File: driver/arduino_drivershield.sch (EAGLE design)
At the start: 35 parts, among them IC1 LB1973M, IC10 LB1973M, IC11 LB1973M, IC12 74HC14D, IC2 LB1973M, IC3 74HC14D, IC4 LB1973M, IC5 LB1973M, IC6 74HC14D, IC7 LB1973M, IC8 LB1973M, IC9 74HC14D, J1 J5MM, J2 J5MM, U1 ARDUINO_SHIELDLABEL

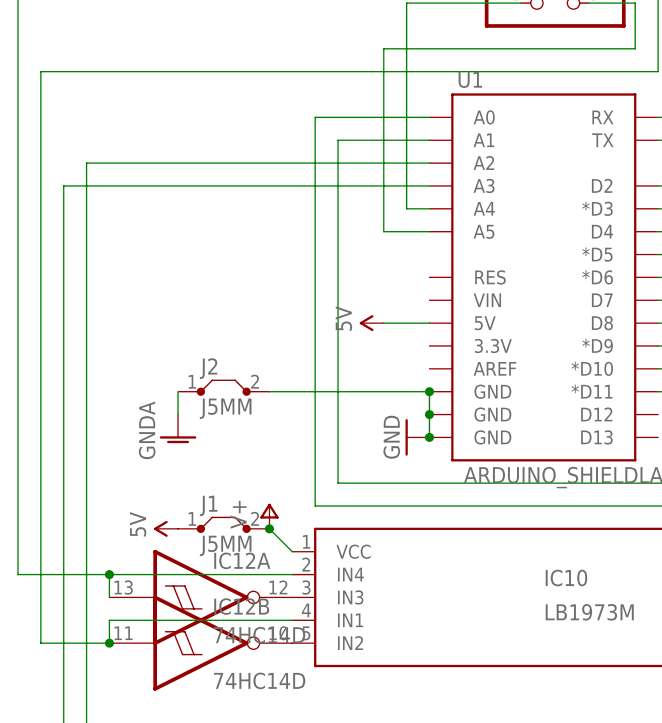
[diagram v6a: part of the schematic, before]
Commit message: added some more jumper to hopefully get better ground connections
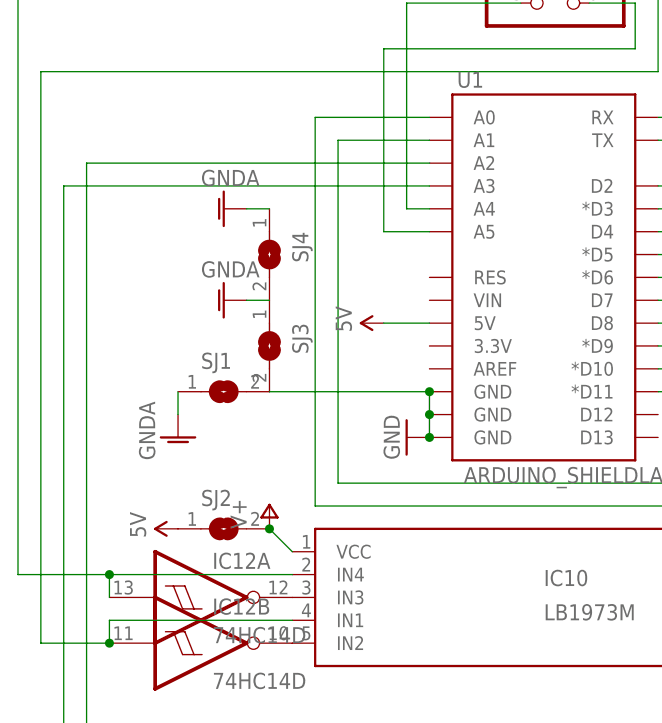
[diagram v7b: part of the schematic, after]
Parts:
- removed J1, J2: J5MM, jumper:J5MM
- added SJ1, SJ2, SJ3, SJ4: (no value), jumper:SJ
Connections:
- removed net GND@2: C10.1, C11.1, C9.1, IC12C.I, IC12D.I, IC12P.GND, IC3C.I, IC3D.I, IC3P.GND, IC6C.I, IC6D.I, IC6P.GND, IC9C.I, IC9D.I, IC9P.GND, J2.2, U1.GND@0, U1.GND@1, U1.GND@2
- removed net GND@3: C1.2, C2.2, C3.2, C4.2, C5.2, C6.2, C7.2, C8.2, IC1.GND, IC10.GND, IC11.GND, IC2.GND, IC4.GND, IC5.GND, IC7.GND, IC8.GND, J2.1
- new net FOO: C1.2, C2.2, C3.2, C4.2, C5.2, C6.2, C7.2, C8.2, IC1.GND, IC11.GND, IC2.GND, IC4.GND, IC5.GND, IC7.GND, IC8.GND, SJ1.1, SJ3.1, SJ4.1
- new net GND: C10.1, C11.1, C9.1, IC12C.I, IC12D.I, IC12P.GND, IC3C.I, IC3D.I, IC3P.GND, IC6C.I, IC6D.I, IC6P.GND, IC9C.I, IC9D.I, IC9P.GND, SJ1.2, U1.GND@0, U1.GND@1, U1.GND@2
- new net GND@PWR: IC10.GND
- net 5V: now also SJ2.1
- net 5V@1: no longer J1.1
- net V+: now also SJ2.2; no longer J1.2
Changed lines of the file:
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@@
 <part name="P+7" library="supply1" deviceset="V+" device=""/>
 <part name="P+8" library="supply1" deviceset="V+" device=""/>
-<part name="J1" library="jumper" deviceset="J" device="5MM"/>
 <part name="U$3" library="SparkFun-Aesthetics" deviceset="5V" device=""/>
 <part name="GND14" library="supply1" deviceset="GNDA" device=""/>
@@
 <part name="P+15" library="supply1" deviceset="V+" device=""/>
 <part name="P+16" library="supply1" deviceset="V+" device=""/>
-<part name="J2" library="jumper" deviceset="J" device="5MM"/>
 <part name="GND9" library="supply1" deviceset="GNDA" device=""/>
 <part name="C9" library="rcl" deviceset="C-EU" device="C0805"/>
@@
 <part name="U$5" library="SparkFun-Aesthetics" deviceset="5V" device=""/>
 <part name="U$6" library="SparkFun-Aesthetics" deviceset="5V" device=""/>
+<part name="SJ1" library="jumper" deviceset="SJ" device=""/>
+<part name="SJ2" library="jumper" deviceset="SJ" device=""/>
+<part name="GND23" library="supply1" deviceset="GNDA" device=""/>
+<part name="SJ3" library="jumper" deviceset="SJ" device=""/>
+<part name="GND24" library="supply1" deviceset="GNDA" device=""/>
+<part name="SJ4" library="jumper" deviceset="SJ" device=""/>
 </parts>
 <sheets>
@@
 <instance part="P+7" gate="1" x="-2.54" y="-20.32"/>
 <instance part="P+8" gate="1" x="-5.08" y="5.08"/>
-<instance part="J1" gate="1" x="-10.16" y="2.54"/>
 <instance part="U$3" gate="G$1" x="-15.24" y="2.54" rot="R90"/>
 <instance part="GND14" gate="1" x="60.96" y="-35.56"/>
@@
 <instance part="P+15" gate="1" x="73.66" y="-20.32"/>
 <instance part="P+16" gate="1" x="73.66" y="2.54"/>
-<instance part="J2" gate="1" x="-10.16" y="17.78"/>
 <instance part="GND9" gate="1" x="-15.24" y="12.7"/>
 <instance part="C9" gate="G$1" x="58.42" y="109.22"/>
@@
 <instance part="U$5" gate="G$1" x="99.06" y="104.14" rot="R90"/>
 <instance part="U$6" gate="G$1" x="132.08" y="104.14" rot="R90"/>
+<instance part="SJ1" gate="1" x="-10.16" y="17.78"/>
+<instance part="SJ2" gate="1" x="-10.16" y="2.54"/>
+<instance part="GND23" gate="1" x="-10.16" y="27.94" rot="R270"/>
+<instance part="SJ3" gate="1" x="-5.08" y="22.86" rot="R270"/>
+<instance part="GND24" gate="1" x="-10.16" y="38.1" rot="R270"/>
+<instance part="SJ4" gate="1" x="-5.08" y="33.02" rot="R270"/>
 </instances>
 <busses>
@@
 <pinref part="IC12" gate="P" pin="VCC"/>
 <pinref part="U$13" gate="G$1" pin="5V"/>
-</segment>
-<segment>
-<pinref part="J1" gate="1" pin="1"/>
-<pinref part="U$3" gate="G$1" pin="5V"/>
 </segment>
 </net>
@@
 <pinref part="P+8" gate="1" pin="V+"/>
 <wire x1="-5.08" y1="2.54" x2="-2.54" y2="0" width="0.1524" layer="91"/>
-<pinref part="J1" gate="1" pin="2"/>
+<pinref part="SJ2" gate="1" pin="2"/>
 <junction x="-5.08" y="2.54"/>
 </segment>
@@
 </segment>
 </net>
-<net name="GND@3" class="1">
-<segment>
-<pinref part="IC10" gate="G$1" pin="GND"/>
-<pinref part="GND6" gate="1" pin="GNDA"/>
-<wire x1="60.96" y1="-12.7" x2="58.42" y2="-10.16" width="0.1524" layer="91"/>
-</segment>
+<net name="FOO" class="1">
 <segment>
 <pinref part="IC8" gate="G$1" pin="GND"/>
@@
 </segment>
 <segment>
-<pinref part="J2" gate="1" pin="1"/>
 <pinref part="GND9" gate="1" pin="GNDA"/>
 <wire x1="-15.24" y1="15.24" x2="-15.24" y2="17.78" width="0.1524" layer="91"/>
-</segment>
-</net>
-<net name="GND@2" class="0">
+<pinref part="SJ1" gate="1" pin="1"/>
+</segment>
+<segment>
+<pinref part="GND23" gate="1" pin="GNDA"/>
+<wire x1="-7.62" y1="27.94" x2="-5.08" y2="27.94" width="0.1524" layer="91"/>
+<pinref part="SJ3" gate="1" pin="1"/>
+</segment>
+<segment>
+<pinref part="GND24" gate="1" pin="GNDA"/>
+<wire x1="-7.62" y1="38.1" x2="-5.08" y2="38.1" width="0.1524" layer="91"/>
+<pinref part="SJ4" gate="1" pin="1"/>
+</segment>
+</net>
+<net name="GND" class="0">
 <segment>
 <pinref part="U1" gate="G$1" pin="GND@0"/>
@@
 <junction x="12.7" y="17.78"/>
 <junction x="12.7" y="15.24"/>
-<pinref part="J2" gate="1" pin="2"/>
+<pinref part="SJ1" gate="1" pin="2"/>
 </segment>
 <segment>
@@
 <wire x1="7.62" y1="25.4" x2="12.7" y2="25.4" width="0.1524" layer="91"/>
 </segment>
-</net>
+<segment>
+<pinref part="U$3" gate="G$1" pin="5V"/>
+<pinref part="SJ2" gate="1" pin="1"/>
+</segment>
+</net>
+<net name="GND@PWR" class="1">
+<segment>
+<pinref part="IC10" gate="G$1" pin="GND"/>
+<pinref part="GND6" gate="1" pin="GNDA"/>
+<wire x1="60.96" y1="-12.7" x2="58.42" y2="-10.16" width="0.1524" layer="91"/>
+</segment>
+</net>

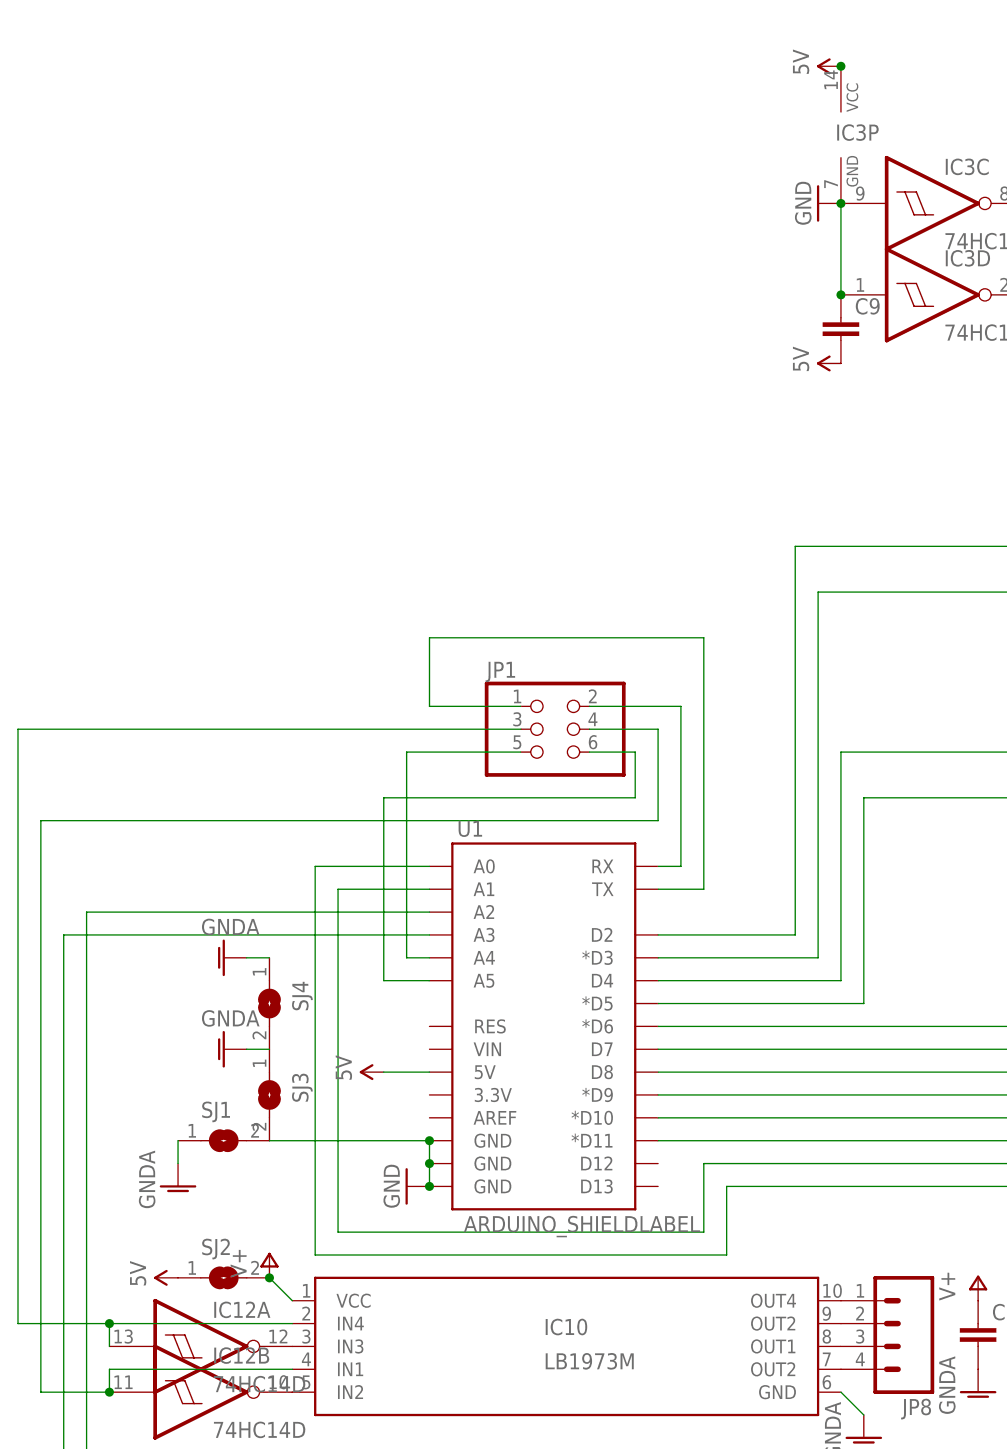
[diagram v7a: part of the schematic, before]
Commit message: crap, there was still a leftover from myh signal namig adventures
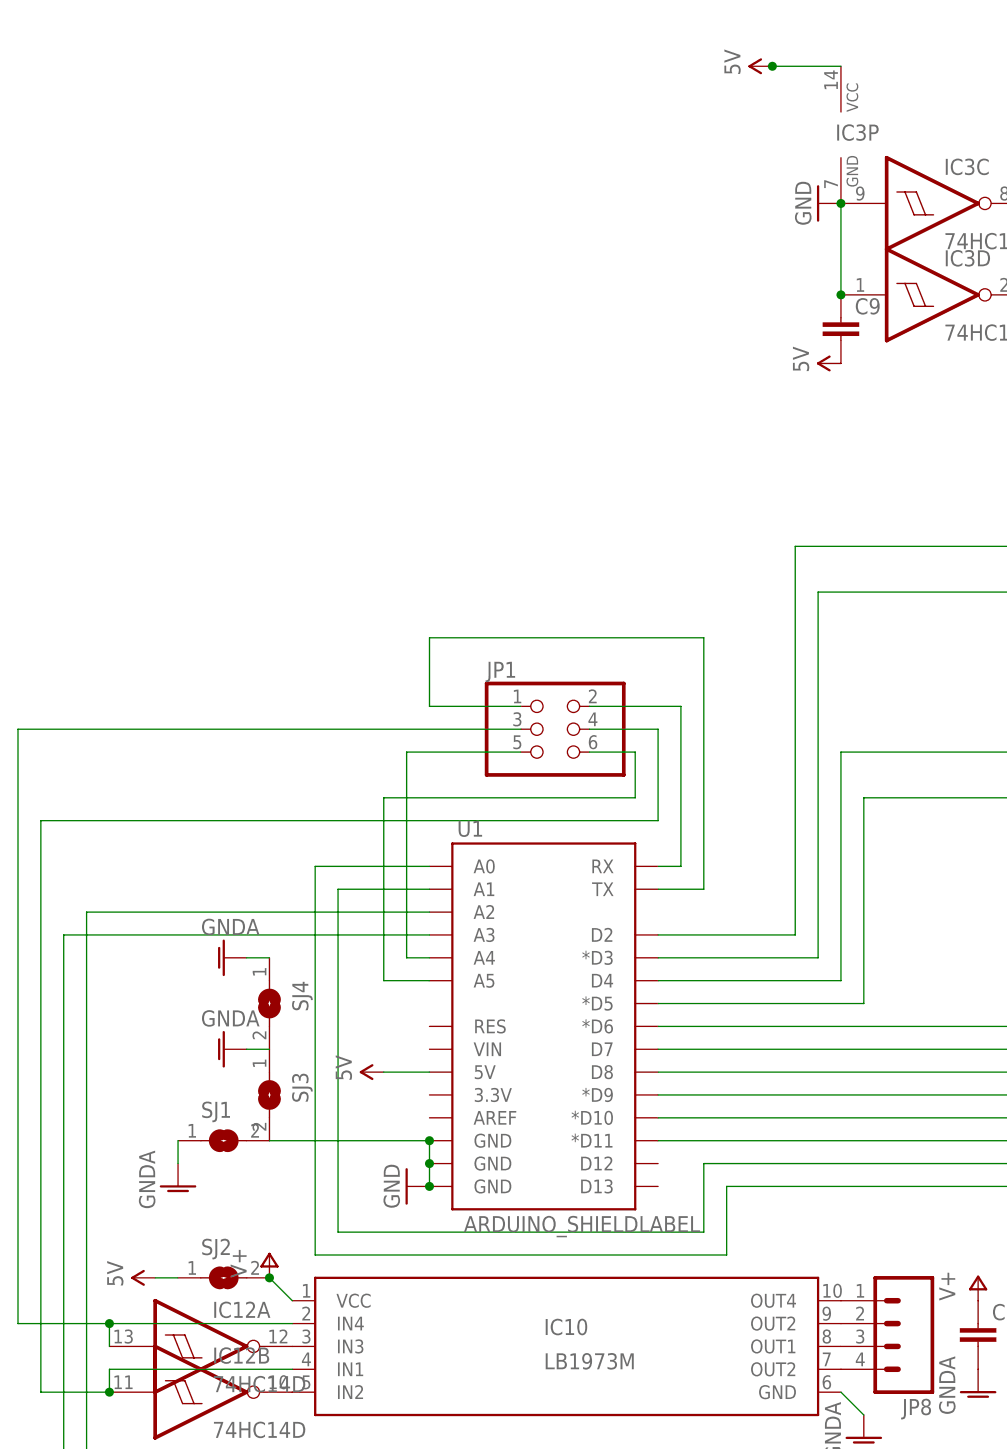
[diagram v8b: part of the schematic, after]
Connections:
- removed net 5V@1: IC12P.VCC, IC3P.VCC, IC6P.VCC, IC9P.VCC
- net 5V: now also IC12P.VCC, IC3P.VCC, IC6P.VCC, IC9P.VCC
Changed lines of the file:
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@@
 <instance part="IC3" gate="P" x="58.42" y="129.54"/>
 <instance part="GND10" gate="1" x="55.88" y="121.92" rot="R270"/>
-<instance part="U$2" gate="G$1" x="58.42" y="137.16" rot="R90"/>
+<instance part="U$2" gate="G$1" x="50.8" y="137.16" rot="R90"/>
 <instance part="JP4" gate="G$1" x="185.42" y="30.48" rot="R180"/>
 <instance part="JP5" gate="G$1" x="185.42" y="7.62" rot="R180"/>
@@
 <instance part="P+7" gate="1" x="-2.54" y="-20.32"/>
 <instance part="P+8" gate="1" x="-5.08" y="5.08"/>
-<instance part="U$3" gate="G$1" x="-15.24" y="2.54" rot="R90"/>
+<instance part="U$3" gate="G$1" x="-17.78" y="2.54" rot="R90"/>
 <instance part="GND14" gate="1" x="60.96" y="-35.56"/>
 <instance part="GND6" gate="1" x="60.96" y="-15.24"/>
@@
 </segment>
 </net>
-<net name="5V@1" class="0">
-<segment>
-<pinref part="IC3" gate="P" pin="VCC"/>
-<pinref part="U$2" gate="G$1" pin="5V"/>
-<pinref part="U$2" gate="G$1" pin="5V"/>
-<junction x="58.42" y="137.16"/>
-</segment>
-<segment>
-<pinref part="IC6" gate="P" pin="VCC"/>
-<pinref part="U$11" gate="G$1" pin="5V"/>
-</segment>
-<segment>
-<pinref part="IC9" gate="P" pin="VCC"/>
-<pinref part="U$12" gate="G$1" pin="5V"/>
-</segment>
-<segment>
-<pinref part="IC12" gate="P" pin="VCC"/>
-<pinref part="U$13" gate="G$1" pin="5V"/>
-</segment>
-</net>
 <net name="N$1" class="0">
 <segment>
@@
 <pinref part="U$3" gate="G$1" pin="5V"/>
 <pinref part="SJ2" gate="1" pin="1"/>
-</segment>
-</net>
+<wire x1="-17.78" y1="2.54" x2="-15.24" y2="2.54" width="0.1524" layer="91"/>
+</segment>
+<segment>
+<pinref part="IC3" gate="P" pin="VCC"/>
+<pinref part="U$2" gate="G$1" pin="5V"/>
+<pinref part="U$2" gate="G$1" pin="5V"/>
+<junction x="50.8" y="137.16"/>
+<wire x1="50.8" y1="137.16" x2="58.42" y2="137.16" width="0.1524" layer="91"/>
+</segment>
+<segment>
+<pinref part="IC6" gate="P" pin="VCC"/>
+<pinref part="U$11" gate="G$1" pin="5V"/>
+</segment>
+<segment>
+<pinref part="IC9" gate="P" pin="VCC"/>
+<pinref part="U$12" gate="G$1" pin="5V"/>
+</segment>
+<segment>
+<pinref part="IC12" gate="P" pin="VCC"/>
+<pinref part="U$13" gate="G$1" pin="5V"/>
+</segment>
+</net>
